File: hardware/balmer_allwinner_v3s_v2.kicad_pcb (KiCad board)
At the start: 4 copper layers, 60 x 60 mm, 120 parts, among them J1 JAE_SIM_Card_SF72S006, J11 Micro_SD_Card_Ebay, J2 UART, J3 Bus_PCI_Express_Mini, J4 USB_C_Receptacle, J8 HR911105_RJ45, SW2 SW_MEC_5G, U1 AllwinnerV3S, U10 TLV62568DBV, U2 CH340C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

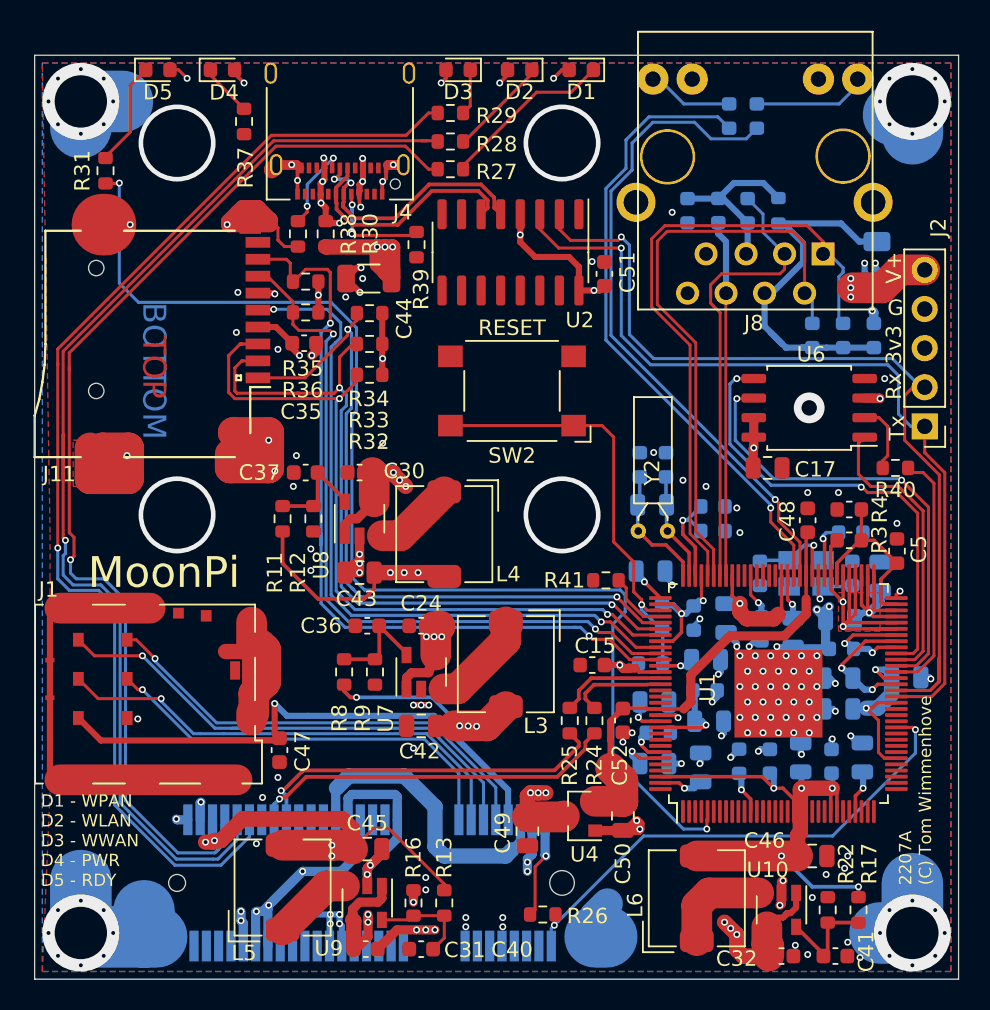
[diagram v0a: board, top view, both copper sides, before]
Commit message: Replaced SD card slot with Wurth 693072010801
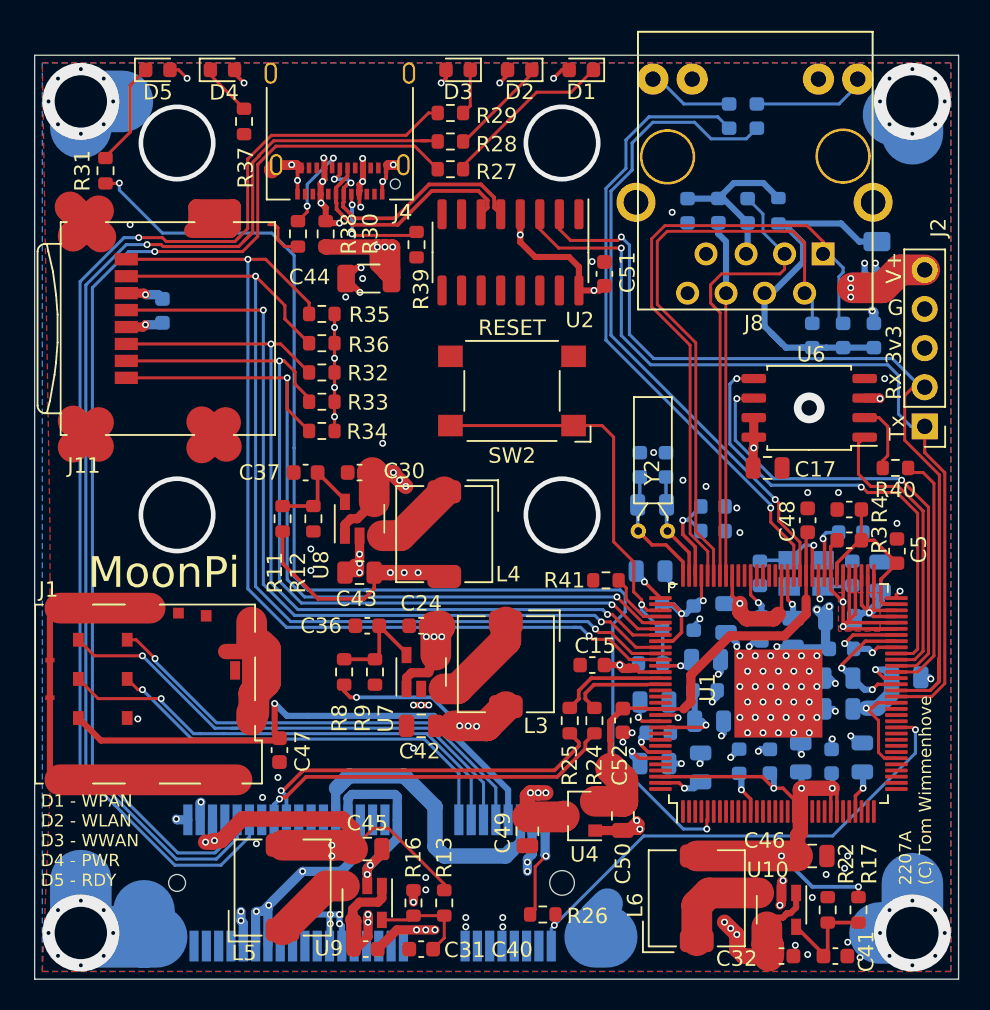
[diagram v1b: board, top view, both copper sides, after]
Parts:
- C35: moved to B.Cu
- J11: value Micro_SD_Card_Ebay -> Micro_SD_Card; footprint balmer:Conn_uSDcard -> Connector_Card:microSD_HC_Wuerth_693072010801
- moved C35 9.44 mm to (70.3, 91.6), turned to 90 degrees
- moved R34 8.25 mm to (80.7, 99.4)
- moved R33 4.87 mm to (80.7, 97.5)
- moved J11 3.64 mm to (69.5, 92.8), turned to 90 degrees
- moved R32 3.10 mm to (80.7, 95.6)
- moved R35 2.35 mm to (80.7, 91.8)
- moved R36 2.26 mm to (80.7, 93.7)
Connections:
- J11 pad 9: Net-(J11-Pad9) -> GND
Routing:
- net SDC0_D0: track 47.9 -> 62.4 mm
- net SDC0_D1: track 53.5 -> 64.1 mm
- net SDC0_CLK: track 46.5 -> 54.2 mm
- net SDC0_D2: track 47.0 -> 53.0 mm
- net SDC0_CMD: track 49.1 -> 54.8 mm
- net SDC0_D3: track 48.9 -> 53.9 mm
- net GND: track 192.9 -> 188.8 mm, vias 174 -> 164
- net Net-(J3-Pad42): track 75.6 -> 77.9 mm
- net Net-(J3-Pad46): track 72.5 -> 73.7 mm
- net SDC1_CLK: track 78.7 -> 77.6 mm
- net +3V3: track 174.2 -> 174.6 mm, vias 32 -> 34
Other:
- board text removed: "BOTTOM"
- board text removed: "TOP"

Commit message: Fixed DRC
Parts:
- moved C35 4.16 mm to (66.2, 91.9)
- moved R32 0.35 mm to (80.7, 96.0)
- moved R35 0.35 mm to (80.7, 92.2)
- moved J11 0.35 mm to (69.5, 93.1)
- moved R33 0.35 mm to (80.7, 97.8)
- moved R34 0.35 mm to (80.7, 99.8)
- moved R36 0.35 mm to (80.7, 94.0)
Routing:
- net Net-(J3-Pad42): track 77.9 -> 79.4 mm
- net Net-(J3-Pad46): track 73.7 -> 75.2 mm
- net Net-(J3-Pad44): track 76.2 -> 77.6 mm
- net GND: track 188.8 -> 188.2 mm
- net +3V3: track 174.6 -> 174.0 mm

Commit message: Forgot some GND vias
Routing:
- net GND: vias 164 -> 168
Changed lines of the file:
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@@
   )
   (setup
-    (last_trace_width 0.6)
+    (last_trace_width 0.2)
     (user_trace_width 0.1778)
     (user_trace_width 0.19177)
@@
   (via (at 112.8 114) (size 0.45) (drill 0.25) (layers F.Cu B.Cu) (net 1))
   (segment (start 103.335469 117.147969) (end 103.1875 117) (width 0.4) (layer B.Cu) (net 1))
-  (via (at 84.6 100.2) (size 0.45) (drill 0.25) (layers F.Cu B.Cu) (net 1))
   (via (at 86.6 120) (size 0.45) (drill 0.25) (layers F.Cu B.Cu) (net 1))
   (via (at 86.6 117.2) (size 0.45) (drill 0.25) (layers F.Cu B.Cu) (net 1))
@@
   (segment (start 66.475 90.8) (end 66.15 91.125) (width 0.6) (layer B.Cu) (net 1))
   (segment (start 67 90.8) (end 66.475 90.8) (width 0.6) (layer B.Cu) (net 1))
+  (via (at 79.5 100.85) (size 0.45) (drill 0.25) (layers F.Cu B.Cu) (net 1))
+  (via (at 80 101.1) (size 0.45) (drill 0.25) (layers F.Cu B.Cu) (net 1))
+  (via (at 79.45 103.35) (size 0.45) (drill 0.25) (layers F.Cu B.Cu) (net 1))
+  (via (at 82.4 100.9) (size 0.45) (drill 0.25) (layers F.Cu B.Cu) (net 1))
+  (via (at 81.2 101.2) (size 0.45) (drill 0.25) (layers F.Cu B.Cu) (net 1))
   (via (at 101.6 109.2) (size 0.45) (drill 0.25) (layers F.Cu B.Cu) (net 2))
   (segment (start 102.6375 110.2375) (end 101.6 109.2) (width 0.2286) (layer F.Cu) (net 2))
@@
   (segment (start 88.175 82.4) (end 86.679822 80.904822) (width 0.2) (layer F.Cu) (net 102))
   (segment (start 73.7 126.8) (end 73.95 126.55) (width 0.2) (layer B.Cu) (net 102))
-  (segment (start 65.8 121.6) (end 71 126.8) (width 0.2) (layer B.Cu) (net 102))
-  (segment (start 65.15 121.6) (end 65.8 121.6) (width 0.2) (layer B.Cu) (net 102))
-  (segment (start 65.15 90.2) (end 65.15 121.6) (width 0.2) (layer B.Cu) (net 102))
+  (segment (start 70.45 126.8) (end 73.7 126.8) (width 0.2) (layer B.Cu) (net 102))
+  (segment (start 65.15 121.5) (end 70.45 126.8) (width 0.2) (layer B.Cu) (net 102))
+  (segment (start 65.15 90.2) (end 65.15 121.5) (width 0.2) (layer B.Cu) (net 102))
   (segment (start 67.25 88.1) (end 65.15 90.2) (width 0.2) (layer B.Cu) (net 102))
   (segment (start 69.8 88.1) (end 67.25 88.1) (width 0.2) (layer B.Cu) (net 102))
-  (segment (start 71 126.8) (end 73.7 126.8) (width 0.2) (layer B.Cu) (net 102))
   (segment (start 88.127411 80.552411) (end 88.175 80.6) (width 0.2) (layer F.Cu) (net 104))
   (segment (start 87.147589 80.552411) (end 88.127411 80.552411) (width 0.2) (layer F.Cu) (net 104))
@@
   (segment (start 75.21455 87.77299) (end 75.24578 87.77299) (width 0.2) (layer F.Cu) (net 104))
   (segment (start 76.161667 86.507103) (end 76.161667 86.857103) (width 0.2) (layer F.Cu) (net 104))
-  (segment (start 64.8 90) (end 64.8 121.712463) (width 0.2) (layer B.Cu) (net 104))
-  (segment (start 73.8 127.2) (end 75.15 125.85) (width 0.2) (layer B.Cu) (net 104))
-  (segment (start 65.014548 121.927011) (end 65.57863 121.927011) (width 0.2) (layer B.Cu) (net 104))
   (segment (start 75.15 125.85) (end 75.15 124.65) (width 0.2) (layer B.Cu) (net 104))
-  (segment (start 65.57863 121.927011) (end 70.851619 127.2) (width 0.2) (layer B.Cu) (net 104))
-  (segment (start 64.8 121.712463) (end 65.014548 121.927011) (width 0.2) (layer B.Cu) (net 104))
+  (segment (start 73.8 127.2) (end 75.15 125.85) (width 0.2) (layer B.Cu) (net 104))
+  (segment (start 70.4 127.2) (end 73.8 127.2) (width 0.2) (layer B.Cu) (net 104))
+  (segment (start 70.35 127.2) (end 70.4 127.2) (width 0.2) (layer B.Cu) (net 104))
+  (segment (start 64.8 121.65) (end 70.35 127.2) (width 0.2) (layer B.Cu) (net 104))
+  (segment (start 64.8 90) (end 64.8 121.65) (width 0.2) (layer B.Cu) (net 104))
   (segment (start 67.152 87.648) (end 64.8 90) (width 0.2) (layer B.Cu) (net 104))
-  (segment (start 70.851619 127.2) (end 73.8 127.2) (width 0.2) (layer B.Cu) (net 104))
   (segment (start 69.299022 87.648) (end 67.152 87.648) (width 0.2) (layer B.Cu) (net 104))
   (via (at 68.762101 87.196) (size 0.45) (drill 0.25) (layers F.Cu B.Cu) (net 105))
@@
   (segment (start 71.3 127.6) (end 71.103235 127.6) (width 0.2) (layer B.Cu) (net 105))
   (segment (start 74.1 127.6) (end 71.3 127.6) (width 0.2) (layer B.Cu) (net 105))
-  (segment (start 64.45 121.824926) (end 64.45 89.8) (width 0.2) (layer B.Cu) (net 105))
-  (segment (start 70.75 127.6) (end 65.404022 122.254022) (width 0.2) (layer B.Cu) (net 105))
-  (segment (start 65.404022 122.254022) (end 64.879096 122.254022) (width 0.2) (layer B.Cu) (net 105))
-  (segment (start 71.3 127.6) (end 70.75 127.6) (width 0.2) (layer B.Cu) (net 105))
-  (segment (start 64.879096 122.254022) (end 64.45 121.824926) (width 0.2) (layer B.Cu) (net 105))
-  (segment (start 67.054 87.196) (end 68.762101 87.196) (width 0.2) (layer B.Cu) (net 105))
   (segment (start 64.45 89.8) (end 67.054 87.196) (width 0.2) (layer B.Cu) (net 105))
+  (segment (start 67.054 87.196) (end 68.762101 87.196) (width 0.2) (layer B.Cu) (net 105))
+  (segment (start 64.45 121.824926) (end 64.45 89.8) (width 0.2) (layer B.Cu) (net 105))
+  (segment (start 70.225074 127.6) (end 64.45 121.824926) (width 0.2) (layer B.Cu) (net 105))
+  (segment (start 71.3 127.6) (end 70.225074 127.6) (width 0.2) (layer B.Cu) (net 105))
   (segment (start 92.6 111.8) (end 92.6 113) (width 2) (layer F.Cu) (net 121))
   (segment (start 89.45 116.15) (end 88.577401 116.15) (width 2) (layer F.Cu) (net 121))

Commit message: Some routing improvements
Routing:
- net Net-(J1-PadC2): track 31.0 -> 31.6 mm
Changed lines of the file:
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@@
     (tags resistor)
     (attr smd)
-    (fp_text reference R40 (at 0 -1.43) (layer F.SilkS)
+    (fp_text reference R40 (at 2.85 -0.05) (layer F.SilkS)
       (effects (font (size 1 1) (thickness 0.15)))
     )
@@
     (tags capacitor)
     (attr smd)
-    (fp_text reference C17 (at 3.1 0.1) (layer F.SilkS)
+    (fp_text reference C17 (at -3.1 0) (layer F.SilkS)
       (effects (font (size 1 1) (thickness 0.15)))
     )
@@
     (tags resistor)
     (attr smd)
-    (fp_text reference R4 (at -1.98 0.02 90) (layer F.SilkS)
+    (fp_text reference R4 (at -2.35 -0.05 180) (layer F.SilkS)
       (effects (font (size 1 1) (thickness 0.15)))
     )
@@
     (tags resistor)
     (attr smd)
-    (fp_text reference R41 (at -2.7 0) (layer F.SilkS)
+    (fp_text reference R41 (at 0.1 -1.4) (layer F.SilkS)
       (effects (font (size 1 1) (thickness 0.15)))
     )
@@
   (segment (start 91.15 122.246768) (end 87.608054 118.704822) (width 0.2) (layer B.Cu) (net 126))
   (segment (start 91.15 124.65) (end 91.15 122.246768) (width 0.2) (layer B.Cu) (net 126))
-  (segment (start 75.104822 118.704822) (end 73.704822 118.704822) (width 0.2) (layer B.Cu) (net 126))
   (segment (start 87.608054 118.704822) (end 75.104822 118.704822) (width 0.2) (layer B.Cu) (net 126))
   (segment (start 75.104822 118.704822) (end 74.791228 118.704822) (width 0.2) (layer B.Cu) (net 126))
-  (via (at 69 114) (size 0.45) (drill 0.25) (layers F.Cu B.Cu) (net 126))
-  (segment (start 73.704822 118.704822) (end 69 114) (width 0.2) (layer B.Cu) (net 126))
-  (segment (start 65.88 114) (end 64.84 112.96) (width 0.2) (layer F.Cu) (net 126))
-  (segment (start 69 114) (end 65.88 114) (width 0.2) (layer F.Cu) (net 126))
+  (via (at 65.65 113) (size 0.45) (drill 0.25) (layers F.Cu B.Cu) (net 126))
+  (segment (start 64.88 113) (end 64.84 112.96) (width 0.2) (layer F.Cu) (net 126))
+  (segment (start 65.65 113) (end 64.88 113) (width 0.2) (layer F.Cu) (net 126))
+  (segment (start 69.3 114.3) (end 66.95 114.3) (width 0.2) (layer B.Cu) (net 126))
+  (segment (start 73.704822 118.704822) (end 69.3 114.3) (width 0.2) (layer B.Cu) (net 126))
+  (segment (start 66.95 114.3) (end 65.65 113) (width 0.2) (layer B.Cu) (net 126))
+  (segment (start 75.104822 118.704822) (end 73.704822 118.704822) (width 0.2) (layer B.Cu) (net 126))
   (segment (start 87.754027 118.352411) (end 91.95 122.548384) (width 0.2) (layer B.Cu) (net 127))
   (segment (start 91.95 122.548384) (end 91.95 124.65) (width 0.2) (layer B.Cu) (net 127))
-  (segment (start 75.447589 118.352411) (end 73.814871 118.352411) (width 0.2) (layer B.Cu) (net 127))
   (segment (start 75.278261 118.352411) (end 75.447589 118.352411) (width 0.2) (layer B.Cu) (net 127))
   (segment (start 75.447589 118.352411) (end 87.754027 118.352411) (width 0.2) (layer B.Cu) (net 127))
-  (via (at 69.819613 114.180387) (size 0.45) (drill 0.25) (layers F.Cu B.Cu) (net 127))
-  (segment (start 69.819613 114.357153) (end 69.819613 114.180387) (width 0.2) (layer B.Cu) (net 127))
-  (segment (start 73.814871 118.352411) (end 69.819613 114.357153) (width 0.2) (layer B.Cu) (net 127))
-  (segment (start 69.819613 114.180387) (end 68.599226 112.96) (width 0.2) (layer F.Cu) (net 127))
-  (segment (start 68.599226 112.96) (end 68.01 112.96) (width 0.2) (layer F.Cu) (net 127))
-  (segment (start 90.35 124.65) (end 90.35 121.945152) (width 0.2) (layer B.Cu) (net 128))
-  (segment (start 90.35 121.945152) (end 87.462081 119.057233) (width 0.2) (layer B.Cu) (net 128))
-  (segment (start 87.462081 119.057233) (end 74.257233 119.057233) (width 0.2) (layer B.Cu) (net 128))
-  (segment (start 74.257233 119.057233) (end 72.742767 119.057233) (width 0.2) (layer B.Cu) (net 128))
-  (segment (start 72.742767 119.057233) (end 72.319693 119.057233) (width 0.2) (layer B.Cu) (net 128))
-  (via (at 70.219613 116.780387) (size 0.45) (drill 0.25) (layers F.Cu B.Cu) (net 128))
-  (segment (start 70.219613 116.957153) (end 70.219613 116.780387) (width 0.2) (layer B.Cu) (net 128))
-  (segment (start 72.319693 119.057233) (end 70.219613 116.957153) (width 0.2) (layer B.Cu) (net 128))
-  (segment (start 66.120387 116.780387) (end 64.84 115.5) (width 0.2) (layer F.Cu) (net 128))
-  (segment (start 70.219613 116.780387) (end 66.120387 116.780387) (width 0.2) (layer F.Cu) (net 128))
-  (segment (start 89.55 124.65) (end 89.55 121.650002) (width 0.2) (layer B.Cu) (net 129))
-  (segment (start 87.309641 119.409643) (end 74.111259 119.409643) (width 0.2) (layer B.Cu) (net 129))
-  (segment (start 89.55 121.650002) (end 87.309641 119.409643) (width 0.2) (layer B.Cu) (net 129))
-  (segment (start 74.111259 119.409643) (end 72.209643 119.409643) (width 0.2) (layer B.Cu) (net 129))
-  (via (at 69 116.2) (size 0.45) (drill 0.25) (layers F.Cu B.Cu) (net 129))
-  (segment (start 72.209643 119.409643) (end 69 116.2) (width 0.2) (layer B.Cu) (net 129))
-  (segment (start 69 116.2) (end 68.91 116.2) (width 0.2) (layer F.Cu) (net 129))
-  (segment (start 68.71 116.2) (end 68.01 115.5) (width 0.2) (layer F.Cu) (net 129))
-  (segment (start 69 116.2) (end 68.71 116.2) (width 0.2) (layer F.Cu) (net 129))
+  (via (at 68.65 113) (size 0.45) (drill 0.25) (layers F.Cu B.Cu) (net 127))
+  (segment (start 68.05 113) (end 68.01 112.96) (width 0.2) (layer F.Cu) (net 127))
+  (segment (start 68.65 113) (end 68.05 113) (width 0.2) (layer F.Cu) (net 127))
+  (segment (start 68.65 113.18754) (end 68.65 113) (width 0.2) (layer B.Cu) (net 127))
+  (segment (start 73.814871 118.352411) (end 68.65 113.18754) (width 0.2) (layer B.Cu) (net 127))
+  (segment (start 75.447589 118.352411) (end 73.814871 118.352411) (width 0.2) (layer B.Cu) (net 127))
+  (via (at 65.602 115.45) (size 0.45) (drill 0.25) (layers F.Cu B.Cu) (net 128))
+  (segment (start 64.89 115.45) (end 64.84 115.5) (width 0.2) (layer F.Cu) (net 128))
+  (segment (start 65.602 115.45) (end 64.89 115.45) (width 0.2) (layer F.Cu) (net 128))
+  (segment (start 69.16455 114.627011) (end 73.594773 119.057233) (width 0.2) (layer B.Cu) (net 128))
+  (segment (start 65.602 115.45) (end 66.424989 114.627011) (width 0.2) (layer B.Cu) (net 128))
+  (segment (start 90.35 121.945152) (end 90.35 124.65) (width 0.2) (layer B.Cu) (net 128))
+  (segment (start 66.424989 114.627011) (end 69.16455 114.627011) (width 0.2) (layer B.Cu) (net 128))
+  (segment (start 87.462081 119.057233) (end 90.35 121.945152) (width 0.2) (layer B.Cu) (net 128))
+  (segment (start 73.594773 119.057233) (end 87.462081 119.057233) (width 0.2) (layer B.Cu) (net 128))
+  (via (at 68.6 115.55) (size 0.45) (drill 0.25) (layers F.Cu B.Cu) (net 129))
+  (segment (start 68.06 115.55) (end 68.01 115.5) (width 0.2) (layer F.Cu) (net 129))
+  (segment (start 68.6 115.55) (end 68.06 115.55) (width 0.2) (layer F.Cu) (net 129))
+  (segment (start 89.55 121.650002) (end 89.55 124.65) (width 0.2) (layer B.Cu) (net 129))
+  (segment (start 87.309641 119.409643) (end 89.55 121.650002) (width 0.2) (layer B.Cu) (net 129))
+  (segment (start 73.484723 119.409643) (end 87.309641 119.409643) (width 0.2) (layer B.Cu) (net 129))
+  (segment (start 69.62508 115.55) (end 73.484723 119.409643) (width 0.2) (layer B.Cu) (net 129))
+  (segment (start 68.6 115.55) (end 69.62508 115.55) (width 0.2) (layer B.Cu) (net 129))
   (via (at 82.620452 84.712568) (size 0.45) (drill 0.25) (layers F.Cu B.Cu) (net 134))
   (segment (start 82.6 84.73302) (end 82.620452 84.712568) (width 0.2) (layer B.Cu) (net 134))
